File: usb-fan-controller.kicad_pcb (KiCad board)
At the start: 2 copper layers, 92 x 46 mm, 120 parts, among them J1 1054500101, J10 JTAG_CONN, J11 DATA_CONN, J12 BOOT0_MODE, J2 EXTPWR_JACK, J3 EXTPWR, J4 PWR_LED, J5 VBAT, J6 THERMO1, J7 THERMO2, J8 SYS_LED, J9 BOOT1_MODE, M1 470531000, M2 470531000, Q1 2N7002, Q2 2N7002, Q3 AO3401A, Q4 2N7002, Q5 2N7002, Q6 AO3401A, Q7 2N7002, Q8 2N7002, SW1 SW_RESET, U1 TPS61040DBV, U2 BQ24392RSER, U3 SRV05-4-P-T7, U4 HT7533-1, U5 MAX6675ISA+, U6 STM32F103C8T6, U7 MAX6675ISA+, Y1 32.768Hz@12.5pF, Y2 8MHz@20pF

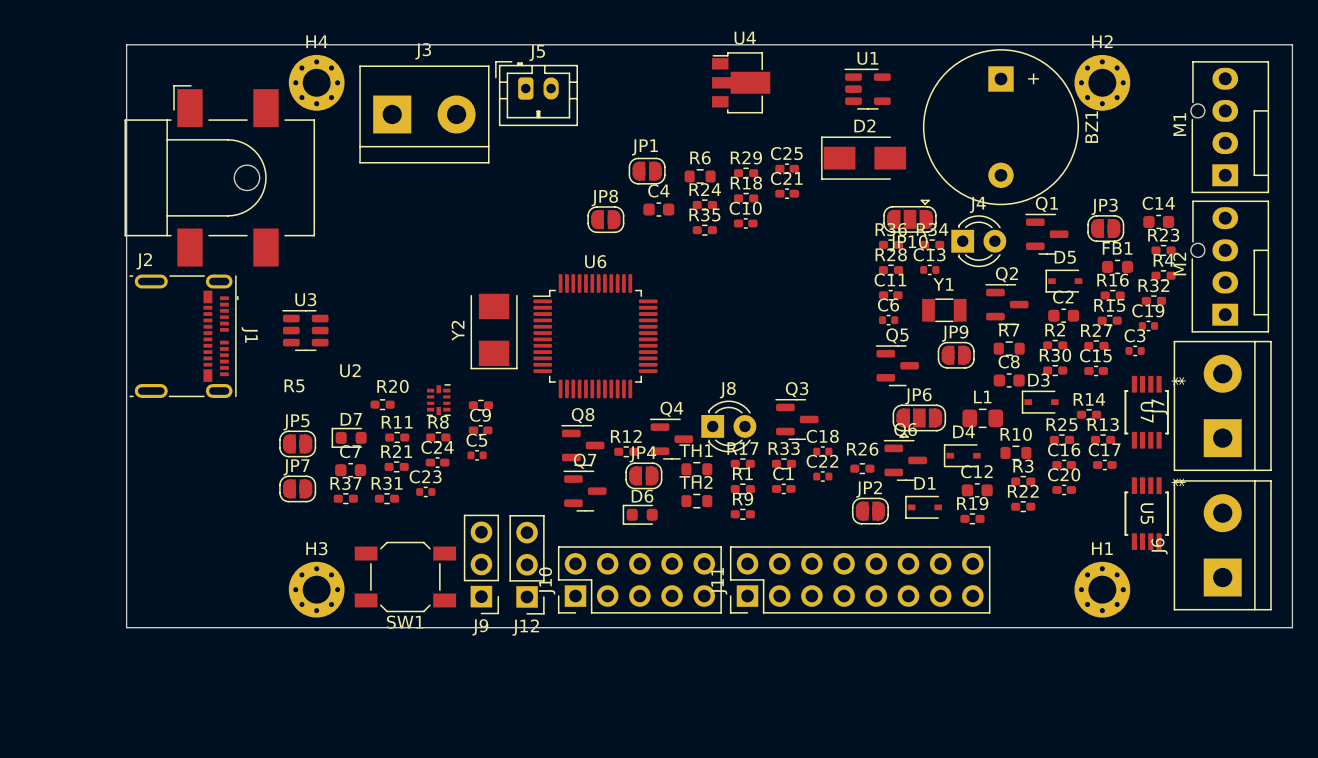
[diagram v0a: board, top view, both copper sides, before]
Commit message: feat: add external THM SPI connection
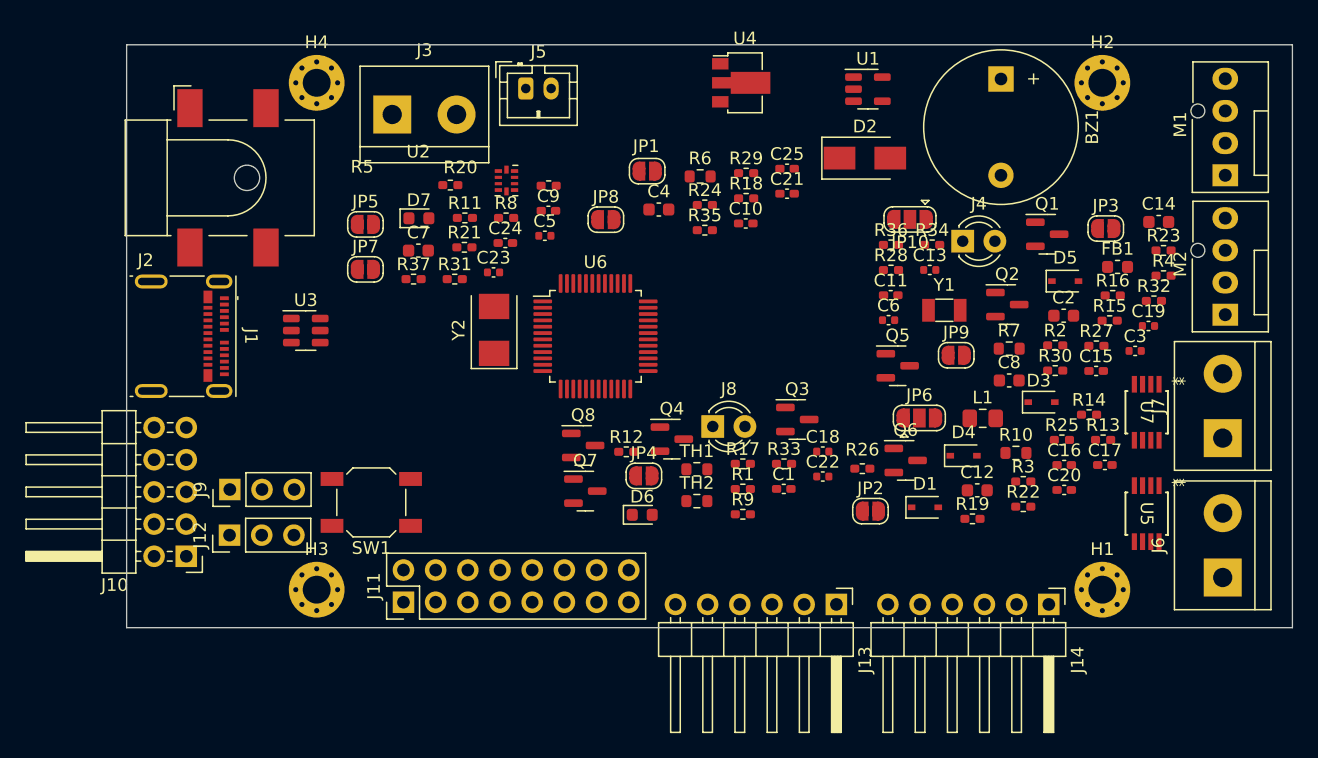
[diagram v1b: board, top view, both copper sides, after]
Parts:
- added J13: THP1_DATA, Connector_PinHeader_2.54mm:PinHeader_1x06_P2.54mm_Horizontal, F.Cu at (151.5, 78.7)
- added J14: THP2_DATA, Connector_PinHeader_2.54mm:PinHeader_1x06_P2.54mm_Horizontal, F.Cu at (168.3, 78.7)
- J10: footprint Connector_PinHeader_2.54mm:PinHeader_2x05_P2.54mm_Vertical -> Connector_PinHeader_2.54mm:PinHeader_2x05_P2.54mm_Horizontal
- J6: value THERMO1 -> THP1_IN
- J7: value THERMO2 -> THP2_IN
- JP8: value THERMO1_MIA -> THP1_MIA
- JP9: value THERMO2_MIA -> THP2_MIA
- moved J10 30.9 mm to (100.2, 74.9), turned to 180 degrees
- moved J11 27.2 mm to (117.3, 78.5)
- moved J12 24.0 mm to (103.6, 73.2), turned to 90 degrees
- moved J9 21.6 mm to (103.6, 69.6), turned to 90 degrees
- moved C9 18.1 mm to (128.8, 47.6)
- moved R20 18.1 mm to (128.8, 45.6)
- moved C23 18.1 mm to (124.5, 52.5)
- moved C5 18.1 mm to (128.5, 49.6)
- moved JP5 18.1 mm to (114.3, 48.7)
- moved R21 18.1 mm to (122.2, 50.5)
- moved D7 18.1 mm to (118.6, 48.2)
- moved JP7 18.1 mm to (114.3, 52.2)
- moved R11 18.1 mm to (122.2, 48.2)
- moved R31 18.1 mm to (121.4, 53.0)
- moved R37 18.1 mm to (118.1, 53.0)
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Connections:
- net 12V_IN_DET renamed EXT12V_DET
- net INTERRUPT renamed INT_OUT
- net SPI_CLK renamed EXTSPI_SCK
- net SPI_CS renamed EXTSPI_CS
- net SPI_MISO renamed EXTSPI_MISO
- net SPI_MOSI renamed EXTSPI_MOSI
- J11 pad 2: I2C_SDA -> EXTI2C_SDA
- J11 pad 3: I2C_SCL -> EXTI2C_SCL
- J11 pad 5: TAMPER -> unconnected-(J11-Pad5)
- J7 pad 2: /THERMO2_IN+ -> /THERMO1_IN+
- U6 pad 2: TAMPER -> SYS_LED_EN
- U6 pad 21: USB_CHGDET -> BUZZ_EN
- U6 pad 28: SYS_LED_EN -> THERMO_MOSI
- U6 pad 29: I2C_SCL -> USB_SWOPEN
- U6 pad 30: I2C_SDA -> USB_CHGAL
- U6 pad 31: BUZZ_EN -> USB_CHGDET
- U6 pad 45: USB_SWOPEN -> EXTI2C_SCL
- U6 pad 46: USB_CHGAL -> EXTI2C_SDA
- U7 pad 3: /THERMO2_IN+ -> /THERMO1_IN+
